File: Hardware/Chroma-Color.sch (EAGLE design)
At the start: 44 parts, among them J1 15-91-1102, J2 87832-6422, J3 1775470-6, U1 EP4CE6E22C8N, U2 ADP3338AKCZ-3.3-RL, U3 ADP3338AKCZ-2.5-RL, U4 NCV565ST12T3G, U5 M25P40-VMN6TPBCT, X1 ASDMB-50.000MHZ-LC-T

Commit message: Schematic done, Updated software with latest
Connectors need physical testing before layout happens. DMD connector
needs to be switched to SMT part
D2514-6V0C-AR-WD.
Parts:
- added !CONFIG, RESET: (no value), MF_Switches:TACT_6MM
- added C22, C23: 0.1uF, MF_Passives:CAPACITOR_NP_0603
- added R7: 10K, MF_Passives:RESISTOR_0805
- J1: LABEL03 2.5V -> 3.3V
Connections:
- net I2V renamed 12V
- removed net N$20: J2.PIN26
- new net EVENC-: J2.PIN26, U1G$7.120
- new net RESET: R7.P$2, RESET.P$2, U1G$7.125
- net !CONFIG: now also !CONFIG.P$2
- net 2.5V: now also C23.P$1; no longer J1.PIN3, R2.P$2, R3.P$2, R4.P$1, R5.P$1, R6.P$1, U1G$11.96
- net 3.3V: now also C22.P$1, J1.PIN3, R2.P$2, R3.P$2, R4.P$1, R5.P$1, R6.P$1, R7.P$1, U1G$11.96
- net CLK_50: now also U1G$9.25; no longer U1G$9.24
- net CLOCK: now also U1G$8.144
- net DATA: now also U1G$8.143
- net ENABLE: now also U1G$8.135
- net EVEN0+: now also U1G$4.59
- net EVEN0-: now also U1G$4.60
- net EVEN1+: now also U1G$4.70
- net EVEN1-: now also U1G$4.71
- net EVEN2+: now also U1G$5.85
- net EVEN2-: now also U1G$5.84
- net EVENC+: now also U1G$7.121
- net GND: now also !CONFIG.P$4, C22.P$2, C23.P$2, RESET.P$4
- net LATCH: now also U1G$8.142
- net ODD0+: now also U1G$3.38
- net ODD0-: now also U1G$3.39
- net ODD1+: now also U1G$3.49
- net ODD1-: now also U1G$3.50
- net ODD2+: now also U1G$3.52
- net ODD2-: now also U1G$3.53
- net ODDC+: now also U1G$4.54
- net ODDC-: now also U1G$4.55
- net PWM/EN: now also U1G$1.10
- net REG0: now also U1G$8.137
- net REG1: now also U1G$8.138
- net REG2: now also U1G$8.141
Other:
- moved on the sheet: C1, C10, C11, C12, C13, C14, C15, C16, C17, C18, C19, C2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

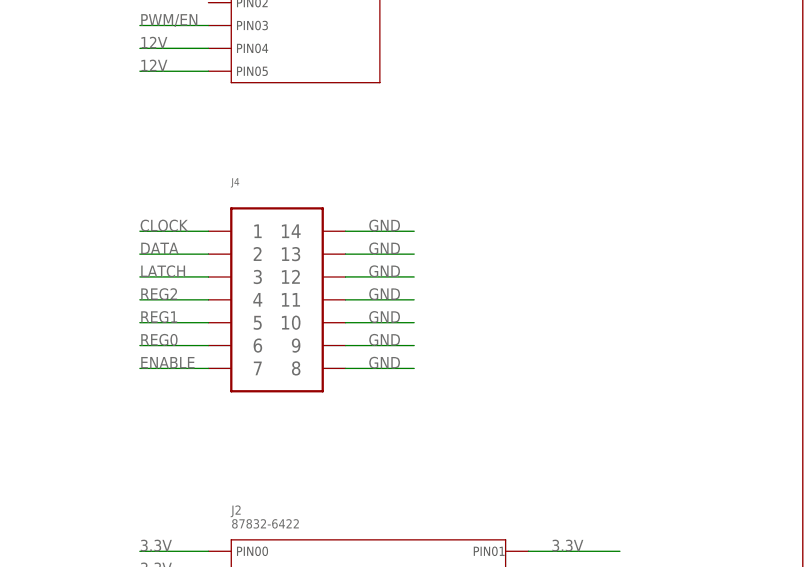
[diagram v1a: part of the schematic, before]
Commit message: Added last 2x7 SMT connector
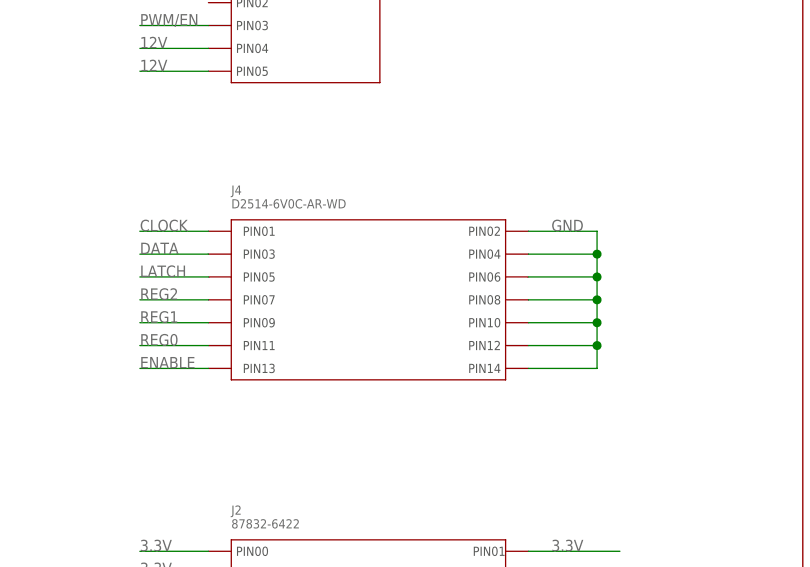
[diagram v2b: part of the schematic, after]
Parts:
- J4: value (none) -> D2514-6V0C-AR-WD; device PP_Connectors:PH_2X07PTH -> PP_Connectors:SMT_02X07D2514-6V0C-AR-WD
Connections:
- net CLOCK: now also J4.PIN1; no longer J4.1
- net DATA: now also J4.PIN3; no longer J4.2
- net ENABLE: now also J4.PIN13; no longer J4.7
- net GND: now also J4.PIN10, J4.PIN12, J4.PIN14, J4.PIN2, J4.PIN4, J4.PIN6, J4.PIN8; no longer J4.10, J4.11, J4.12, J4.13, J4.14, J4.8, J4.9
- net LATCH: now also J4.PIN5; no longer J4.3
- net REG0: now also J4.PIN11; no longer J4.6
- net REG1: now also J4.PIN9; no longer J4.5
- net REG2: now also J4.PIN7; no longer J4.4
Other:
- moved on the sheet: J4
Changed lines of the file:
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@@
 <?xml version="1.0" encoding="utf-8"?>
 <!DOCTYPE eagle SYSTEM "eagle.dtd">
-<eagle version="6.6.0">
+<eagle version="6.5.0">
 <drawing>
 <settings>
@@
 <part name="J2" library="PP_Connectors" deviceset="87832-6422" device="" value="87832-6422"/>
 <part name="J3" library="PP_Connectors" deviceset="1775470-6" device="" value="1775470-6"/>
-<part name="J4" library="PP_Connectors" deviceset="PH_2X07" device="PTH"/>
 <part name="C22" library="MF_Passives" deviceset="CAPACITOR_NP" device="_0603" value="0.1uF"/>
 <part name="C23" library="MF_Passives" deviceset="CAPACITOR_NP" device="_0603" value="0.1uF"/>
@@
 <part name="RESET" library="MF_Switches" deviceset="TACT" device="_6MM"/>
 <part name="R7" library="MF_Passives" deviceset="RESISTOR" device="_0805" value="10K"/>
+<part name="J4" library="PP_Connectors" deviceset="SMT_02X07" device="D2514-6V0C-AR-WD" value="D2514-6V0C-AR-WD"/>
 </parts>
 <sheets>
@@
 <instance part="J2" gate="G$1" x="-63.5" y="124.46"/>
 <instance part="J3" gate="G$1" x="-63.5" y="190.5"/>
-<instance part="J4" gate="G$1" x="-58.42" y="152.4"/>
 <instance part="C22" gate="G$1" x="-182.88" y="99.06"/>
 <instance part="C23" gate="G$1" x="-271.78" y="27.94"/>
@@
 <instance part="RESET" gate="G$1" x="-116.84" y="63.5"/>
 <instance part="R7" gate="G$1" x="-254" y="104.14" rot="R270"/>
+<instance part="J4" gate="G$1" x="-63.5" y="160.02"/>
 </instances>
 <busses>
@@
 </segment>
 <segment>
-<pinref part="J4" gate="G$1" pin="14"/>
-<wire x1="-50.8" y1="160.02" x2="-43.18" y2="160.02" width="0.1524" layer="91"/>
-<label x="-48.26" y="160.02" size="1.27" layer="95" font="vector"/>
-</segment>
-<segment>
-<pinref part="J4" gate="G$1" pin="13"/>
-<wire x1="-43.18" y1="157.48" x2="-50.8" y2="157.48" width="0.1524" layer="91"/>
-<label x="-48.26" y="157.48" size="1.27" layer="95" font="vector"/>
-</segment>
-<segment>
-<pinref part="J4" gate="G$1" pin="12"/>
-<wire x1="-50.8" y1="154.94" x2="-43.18" y2="154.94" width="0.1524" layer="91"/>
-<label x="-48.26" y="154.94" size="1.27" layer="95" font="vector"/>
-</segment>
-<segment>
-<pinref part="J4" gate="G$1" pin="11"/>
-<wire x1="-43.18" y1="152.4" x2="-50.8" y2="152.4" width="0.1524" layer="91"/>
-<label x="-48.26" y="152.4" size="1.27" layer="95" font="vector"/>
-</segment>
-<segment>
-<pinref part="J4" gate="G$1" pin="10"/>
-<wire x1="-50.8" y1="149.86" x2="-43.18" y2="149.86" width="0.1524" layer="91"/>
-<label x="-48.26" y="149.86" size="1.27" layer="95" font="vector"/>
-</segment>
-<segment>
-<pinref part="J4" gate="G$1" pin="9"/>
-<wire x1="-43.18" y1="147.32" x2="-50.8" y2="147.32" width="0.1524" layer="91"/>
-<label x="-48.26" y="147.32" size="1.27" layer="95" font="vector"/>
-</segment>
-<segment>
-<pinref part="J4" gate="G$1" pin="8"/>
-<wire x1="-50.8" y1="144.78" x2="-43.18" y2="144.78" width="0.1524" layer="91"/>
-<label x="-48.26" y="144.78" size="1.27" layer="95" font="vector"/>
-</segment>
-<segment>
 <pinref part="!CONFIG" gate="G$1" pin="P$4"/>
 <wire x1="-154.94" y1="60.96" x2="-144.78" y2="60.96" width="0.1524" layer="91"/>
@@
 <wire x1="-111.76" y1="60.96" x2="-101.6" y2="60.96" width="0.1524" layer="91"/>
 <label x="-109.22" y="60.96" size="1.27" layer="95" font="vector"/>
+</segment>
+<segment>
+<pinref part="J4" gate="G$1" pin="PIN2"/>
+<wire x1="-30.48" y1="160.02" x2="-22.86" y2="160.02" width="0.1524" layer="91"/>
+<wire x1="-22.86" y1="160.02" x2="-22.86" y2="157.48" width="0.1524" layer="91"/>
+<pinref part="J4" gate="G$1" pin="PIN14"/>
+<wire x1="-22.86" y1="157.48" x2="-22.86" y2="154.94" width="0.1524" layer="91"/>
+<wire x1="-22.86" y1="154.94" x2="-22.86" y2="152.4" width="0.1524" layer="91"/>
+<wire x1="-22.86" y1="152.4" x2="-22.86" y2="149.86" width="0.1524" layer="91"/>
+<wire x1="-22.86" y1="149.86" x2="-22.86" y2="147.32" width="0.1524" layer="91"/>
+<wire x1="-22.86" y1="147.32" x2="-22.86" y2="144.78" width="0.1524" layer="91"/>
+<wire x1="-22.86" y1="144.78" x2="-30.48" y2="144.78" width="0.1524" layer="91"/>
+<pinref part="J4" gate="G$1" pin="PIN12"/>
+<wire x1="-30.48" y1="147.32" x2="-22.86" y2="147.32" width="0.1524" layer="91"/>
+<pinref part="J4" gate="G$1" pin="PIN10"/>
+<wire x1="-30.48" y1="149.86" x2="-22.86" y2="149.86" width="0.1524" layer="91"/>
+<pinref part="J4" gate="G$1" pin="PIN8"/>
+<wire x1="-30.48" y1="152.4" x2="-22.86" y2="152.4" width="0.1524" layer="91"/>
+<pinref part="J4" gate="G$1" pin="PIN6"/>
+<wire x1="-30.48" y1="154.94" x2="-22.86" y2="154.94" width="0.1524" layer="91"/>
+<pinref part="J4" gate="G$1" pin="PIN4"/>
+<wire x1="-30.48" y1="157.48" x2="-22.86" y2="157.48" width="0.1524" layer="91"/>
+<junction x="-22.86" y="157.48"/>
+<junction x="-22.86" y="154.94"/>
+<junction x="-22.86" y="152.4"/>
+<junction x="-22.86" y="149.86"/>
+<junction x="-22.86" y="147.32"/>
+<label x="-27.94" y="160.02" size="1.27" layer="95" font="vector"/>
 </segment>
 </net>
@@
 <net name="ENABLE" class="0">
 <segment>
-<pinref part="J4" gate="G$1" pin="7"/>
 <wire x1="-66.04" y1="144.78" x2="-73.66" y2="144.78" width="0.1524" layer="91"/>
 <label x="-73.66" y="144.78" size="1.27" layer="95" font="vector"/>
+<pinref part="J4" gate="G$1" pin="PIN13"/>
 </segment>
 <segment>
@@
 <net name="REG0" class="0">
 <segment>
-<pinref part="J4" gate="G$1" pin="6"/>
 <wire x1="-73.66" y1="147.32" x2="-66.04" y2="147.32" width="0.1524" layer="91"/>
 <label x="-73.66" y="147.32" size="1.27" layer="95" font="vector"/>
+<pinref part="J4" gate="G$1" pin="PIN11"/>
 </segment>
 <segment>
@@
 <net name="REG1" class="0">
 <segment>
-<pinref part="J4" gate="G$1" pin="5"/>
 <wire x1="-73.66" y1="149.86" x2="-66.04" y2="149.86" width="0.1524" layer="91"/>
 <label x="-73.66" y="149.86" size="1.27" layer="95" font="vector"/>
+<pinref part="J4" gate="G$1" pin="PIN9"/>
 </segment>
 <segment>
@@
 <net name="REG2" class="0">
 <segment>
-<pinref part="J4" gate="G$1" pin="4"/>
 <wire x1="-66.04" y1="152.4" x2="-73.66" y2="152.4" width="0.1524" layer="91"/>
 <label x="-73.66" y="152.4" size="1.27" layer="95" font="vector"/>
+<pinref part="J4" gate="G$1" pin="PIN7"/>
 </segment>
 <segment>
@@
 <net name="LATCH" class="0">
 <segment>
-<pinref part="J4" gate="G$1" pin="3"/>
 <wire x1="-73.66" y1="154.94" x2="-66.04" y2="154.94" width="0.1524" layer="91"/>
 <label x="-73.66" y="154.94" size="1.27" layer="95" font="vector"/>
+<pinref part="J4" gate="G$1" pin="PIN5"/>
 </segment>
 <segment>
@@
 <net name="DATA" class="0">
 <segment>
-<pinref part="J4" gate="G$1" pin="2"/>
 <wire x1="-66.04" y1="157.48" x2="-73.66" y2="157.48" width="0.1524" layer="91"/>
 <label x="-73.66" y="157.48" size="1.27" layer="95" font="vector"/>
+<pinref part="J4" gate="G$1" pin="PIN3"/>
 </segment>
 <segment>
@@
 <net name="CLOCK" class="0">
 <segment>
-<pinref part="J4" gate="G$1" pin="1"/>
 <wire x1="-66.04" y1="160.02" x2="-73.66" y2="160.02" width="0.1524" layer="91"/>
 <label x="-73.66" y="160.02" size="1.27" layer="95" font="vector"/>
-</segment>
-<segment>
+<pinref part="J4" gate="G$1" pin="PIN1"/>
+</segment>
+<segment>

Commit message: Started Routing.
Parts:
- added J5, J6: (no value), MF_Connectors:HEADER_01X34_PTH_2.54MM
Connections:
- new net PIN_1: J5.PIN0, U1G$1.1
- new net PIN_100: J6.PIN3, U1G$6.100
- new net PIN_101: J6.PIN4, U1G$6.101
- new net PIN_103: J6.PIN5, U1G$6.103
- new net PIN_104: J6.PIN6, U1G$6.104
- new net PIN_105: J6.PIN7, U1G$6.105
- new net PIN_106: J6.PIN8, U1G$6.106
- new net PIN_11: J5.PIN4, U1G$1.11
- new net PIN_110: J6.PIN9, U1G$7.110
- new net PIN_111: J6.PIN10, U1G$7.111
- new net PIN_112: J6.PIN11, U1G$7.112
- new net PIN_113: J6.PIN12, U1G$7.113
- new net PIN_114: J6.PIN13, U1G$7.114
- new net PIN_115: J6.PIN14, U1G$7.115
- new net PIN_119: J6.PIN15, U1G$7.119
- new net PIN_124: J6.PIN16, U1G$7.124
- new net PIN_126: J6.PIN17, U1G$7.126
- new net PIN_127: J6.PIN18, U1G$7.127
- new net PIN_128: J6.PIN19, U1G$8.128
- new net PIN_129: J6.PIN20, U1G$8.129
- new net PIN_132: J6.PIN21, U1G$8.132
- new net PIN_133: J6.PIN22, U1G$8.133
- new net PIN_136: J6.PIN23, U1G$8.136
- new net PIN_2: J5.PIN1, U1G$1.2
- new net PIN_23: J6.PIN29, U1G$9.23
- new net PIN_24: J6.PIN28, U1G$9.24
- new net PIN_28: J5.PIN5, U1G$2.28
- new net PIN_3: J5.PIN2, U1G$1.3
- new net PIN_30: J5.PIN6, U1G$2.30
- new net PIN_31: J5.PIN7, U1G$2.31
- new net PIN_32: J5.PIN8, U1G$2.32
- new net PIN_33: J5.PIN9, U1G$2.33
- new net PIN_34: J5.PIN10, U1G$2.34
- new net PIN_42: J5.PIN11, U1G$3.42
- new net PIN_43: J5.PIN12, U1G$3.43
- new net PIN_44: J5.PIN13, U1G$3.44
- new net PIN_46: J5.PIN14, U1G$3.46
- new net PIN_51: J5.PIN15, U1G$3.51
- new net PIN_58: J5.PIN16, U1G$4.58
- new net PIN_64: J5.PIN17, U1G$4.64
- new net PIN_65: J5.PIN18, U1G$4.65
- new net PIN_66: J5.PIN19, U1G$4.66
- new net PIN_67: J5.PIN20, U1G$4.67
- new net PIN_68: J5.PIN21, U1G$4.68
- new net PIN_69: J5.PIN22, U1G$4.69
- new net PIN_7: J5.PIN3, U1G$1.7
- new net PIN_72: J5.PIN23, U1G$4.72
- new net PIN_73: J5.PIN24, U1G$5.73
- new net PIN_74: J5.PIN25, U1G$5.74
- new net PIN_75: J5.PIN26, U1G$5.75
- new net PIN_76: J5.PIN27, U1G$5.76
- new net PIN_77: J5.PIN28, U1G$5.77
- new net PIN_80: J5.PIN29, U1G$5.80
- new net PIN_83: J5.PIN30, U1G$5.83
- new net PIN_86: J5.PIN31, U1G$5.86
- new net PIN_87: J6.PIN0, U1G$5.87
- new net PIN_88: J6.PIN24, U1G$9.88
- new net PIN_89: J6.PIN25, U1G$9.89
- new net PIN_90: J6.PIN26, U1G$9.90
- new net PIN_91: J6.PIN27, U1G$9.91
- new net PIN_98: J6.PIN1, U1G$6.98
- new net PIN_99: J6.PIN2, U1G$6.99
- net 3.3V: now also J5.PIN33, J6.PIN33
- net EVEN1+: now also J2.PIN21; no longer J2.PIN20
- net EVEN1-: now also J2.PIN20; no longer J2.PIN21
- net GND: now also J5.PIN32, J6.PIN32
- net ODD2+: now also J2.PIN11; no longer J2.PIN10
- net ODD2-: now also J2.PIN10; no longer J2.PIN11

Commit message: Layout complete. Silkscreen next.
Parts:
- removed J5, J6: (no value), MF_Connectors:HEADER_01X34_PTH_2.54MM
- added C24: 10uF, MF_Passives:CAPACITOR_NP_0603
- added C25, C26, C27, C28, C29, C30, C31, C32, C33, C34, C35, C36, C37, C38: 0.1uF, MF_Passives:CAPACITOR_NP_0603
- added J7: 26-64-4040, PP_Connectors:HEADER_01X03MOLEX_KK_4_P1
- !CONFIG, RESET: device MF_Switches:TACT_6MM -> MF_Switches:TACT_4.2MM
- C16: value 10uF -> 0.1uF
- C9: value 0.1uF -> 100uF; device MF_Passives:CAPACITOR_NP_0603 -> MF_Passives:CAPACITOR_P_6.3MM
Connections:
- net EPCS_!CS renamed !CSO
- net EPCS_ASDI renamed ASDO
- net EPCS_DATA renamed DATA0
- net EP_DCLK renamed DCLK
- net 1.2V: now also C30.P$1, C31.P$1, C32.P$1, C33.P$1, C34.P$1, C35.P$1, C36.P$1, C37.P$1, C38.P$1
- net 12V: now also J7.PIN1
- net 2.5V: now also C10.P$1
- net 3.3V: now also C25.P$1, C26.P$1, C27.P$1, C28.P$1, C29.P$1; no longer J5.PIN33, J6.PIN33
- net 5V: now also C24.P$1, J7.PIN2; no longer C10.P$1
- net GND: now also C24.P$2, C25.P$2, C26.P$2, C27.P$2, C28.P$2, C29.P$2, C30.P$2, C31.P$2, C32.P$2, C33.P$2, C34.P$2, C35.P$2, C36.P$2, C37.P$2, C38.P$2, J7.PIN3; no longer J5.PIN32, J6.PIN32
- net PIN_1: no longer J5.PIN0
- net PIN_100: no longer J6.PIN3
- net PIN_101: no longer J6.PIN4
- net PIN_103: no longer J6.PIN5
- net PIN_104: no longer J6.PIN6
- net PIN_105: no longer J6.PIN7
- net PIN_106: no longer J6.PIN8
- net PIN_11: no longer J5.PIN4
- net PIN_110: no longer J6.PIN9
- net PIN_111: no longer J6.PIN10
- net PIN_112: no longer J6.PIN11
- net PIN_113: no longer J6.PIN12
- net PIN_114: no longer J6.PIN13
- net PIN_115: no longer J6.PIN14
- net PIN_119: no longer J6.PIN15
- net PIN_124: no longer J6.PIN16
- net PIN_126: no longer J6.PIN17
- net PIN_127: no longer J6.PIN18
- net PIN_128: no longer J6.PIN19
- net PIN_129: no longer J6.PIN20
- net PIN_132: no longer J6.PIN21
- net PIN_133: no longer J6.PIN22
- net PIN_136: no longer J6.PIN23
- net PIN_2: no longer J5.PIN1
- net PIN_23: no longer J6.PIN29
- net PIN_24: no longer J6.PIN28
- net PIN_28: no longer J5.PIN5
- net PIN_3: no longer J5.PIN2
- net PIN_30: no longer J5.PIN6
- net PIN_31: no longer J5.PIN7
- net PIN_32: no longer J5.PIN8
- net PIN_33: no longer J5.PIN9
- net PIN_34: no longer J5.PIN10
- net PIN_42: no longer J5.PIN11
- net PIN_43: no longer J5.PIN12
- net PIN_44: no longer J5.PIN13
- net PIN_46: no longer J5.PIN14
- net PIN_51: no longer J5.PIN15
- net PIN_58: no longer J5.PIN16
- net PIN_64: no longer J5.PIN17
- net PIN_65: no longer J5.PIN18
- net PIN_66: no longer J5.PIN19
- net PIN_67: no longer J5.PIN20
- net PIN_68: no longer J5.PIN21
- net PIN_69: no longer J5.PIN22
- net PIN_7: no longer J5.PIN3
- net PIN_72: no longer J5.PIN23
- net PIN_73: no longer J5.PIN24
- net PIN_74: no longer J5.PIN25
- net PIN_75: no longer J5.PIN26
- net PIN_76: no longer J5.PIN27
- net PIN_77: no longer J5.PIN28
- net PIN_80: no longer J5.PIN29
- net PIN_83: no longer J5.PIN30
- net PIN_86: no longer J5.PIN31
- net PIN_87: no longer J6.PIN0
- net PIN_88: no longer J6.PIN24
- net PIN_89: no longer J6.PIN25
- net PIN_90: no longer J6.PIN26
- net PIN_91: no longer J6.PIN27
- net PIN_98: no longer J6.PIN1
- net PIN_99: no longer J6.PIN2
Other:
- moved on the sheet: C1, C10, C11, C12, C13, C14, C15, C16, C17, C18, C19, C2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
